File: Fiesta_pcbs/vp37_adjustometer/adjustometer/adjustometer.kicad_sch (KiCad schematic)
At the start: 25 parts, among them J1 VP37 connector, J2 Output, Q1 BC547, Q2 2SK107, U1 UA78M08, U2 RP2040 Micro

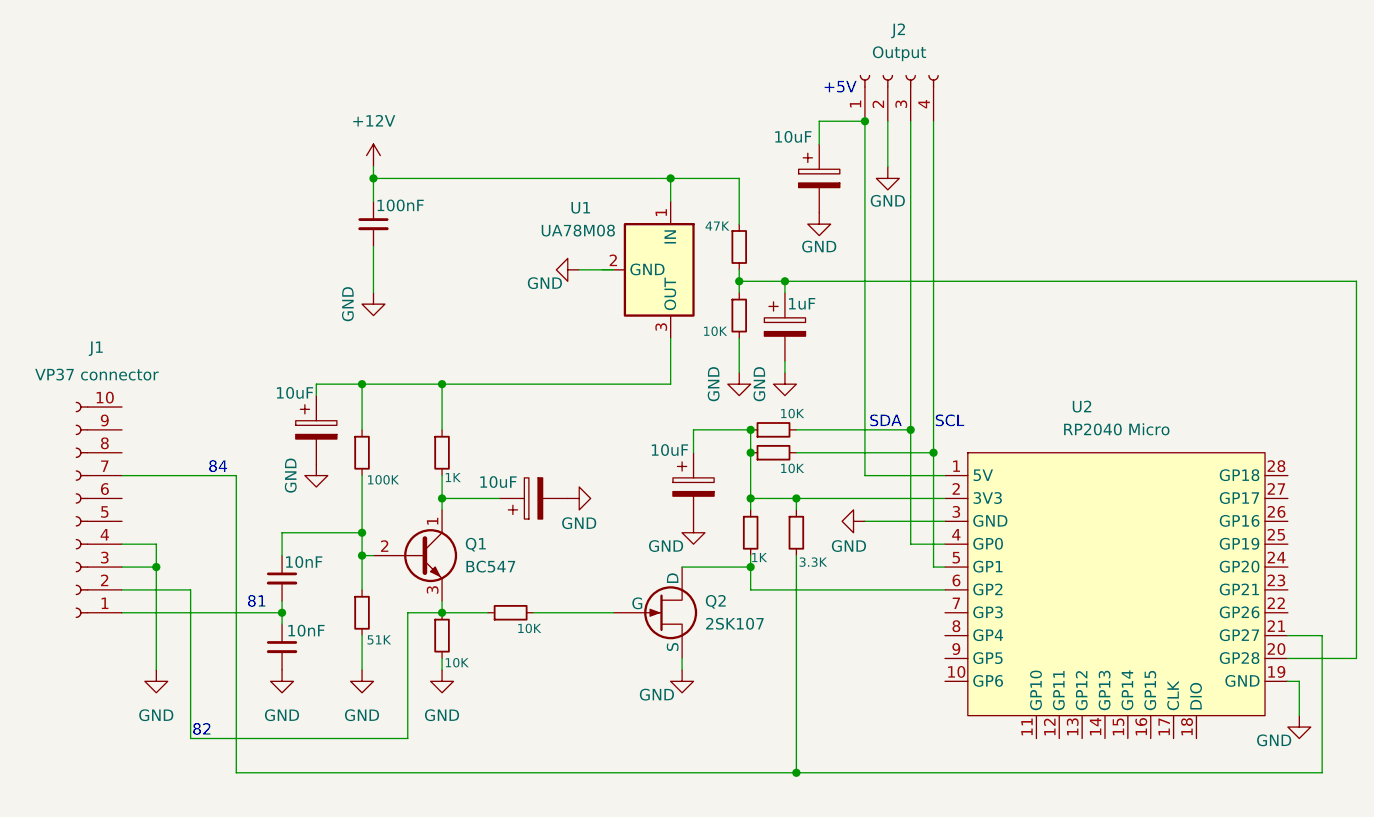
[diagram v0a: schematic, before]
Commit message: sensors, led, start: bitmask status, sequence LED, i2c detection via transaction_count, thermal comp guard
sensors.h/sensors.c:
- Replace AdjStatus enum with bitmask defines: ADJ_STATUS_OK (0x00),
  SIGNAL_LOST (bit 0), FUEL_TEMP_BROKEN (bit 1), BASELINE_PENDING
  (bit 2), VOLTAGE_BAD (bit 3). Multiple bits can be set simultaneously.
- getAdjustometerStatus() returns uint8_t bitmask; checks signal loss,
  baseline readiness, fuel temp raw == 0, and supply voltage outside
  8.0–15.0 V (ADJ_VOLTAGE_MIN_TV / ADJ_VOLTAGE_MAX_TV).
- Thermal compensation now skipped entirely when the fuel temperature
  sensor is broken (raw == ADJ_FUEL_TEMP_SENSOR_BROKEN). Both the EMA
  update and the drift correction are inside the validity guard to
  prevent stale smoothed values from corrupting the drift model.

start.c:
- updateI2CRegisters() reverted to void.
- updateLed() called separately with no arguments.

led.c:
- Detect real I2C activity via hal_i2c_slave_get_transaction_count().
- LED displays a color sequence built additively from active fault
  conditions, each step 500 ms: purple (FUEL_TEMP_BROKEN) and/or red
  (no I2C transactions since last call), always followed by green.
  Signal lost overrides all patterns with 4x/s red blink.
- Steady green at 50% brightness only when all conditions are clear.

config.h: STATUS register comment updated to "status bitmask".

README.md: STATUS register documented as bitmask table with bit
descriptions; LED section updated with combined-sequence behavior.
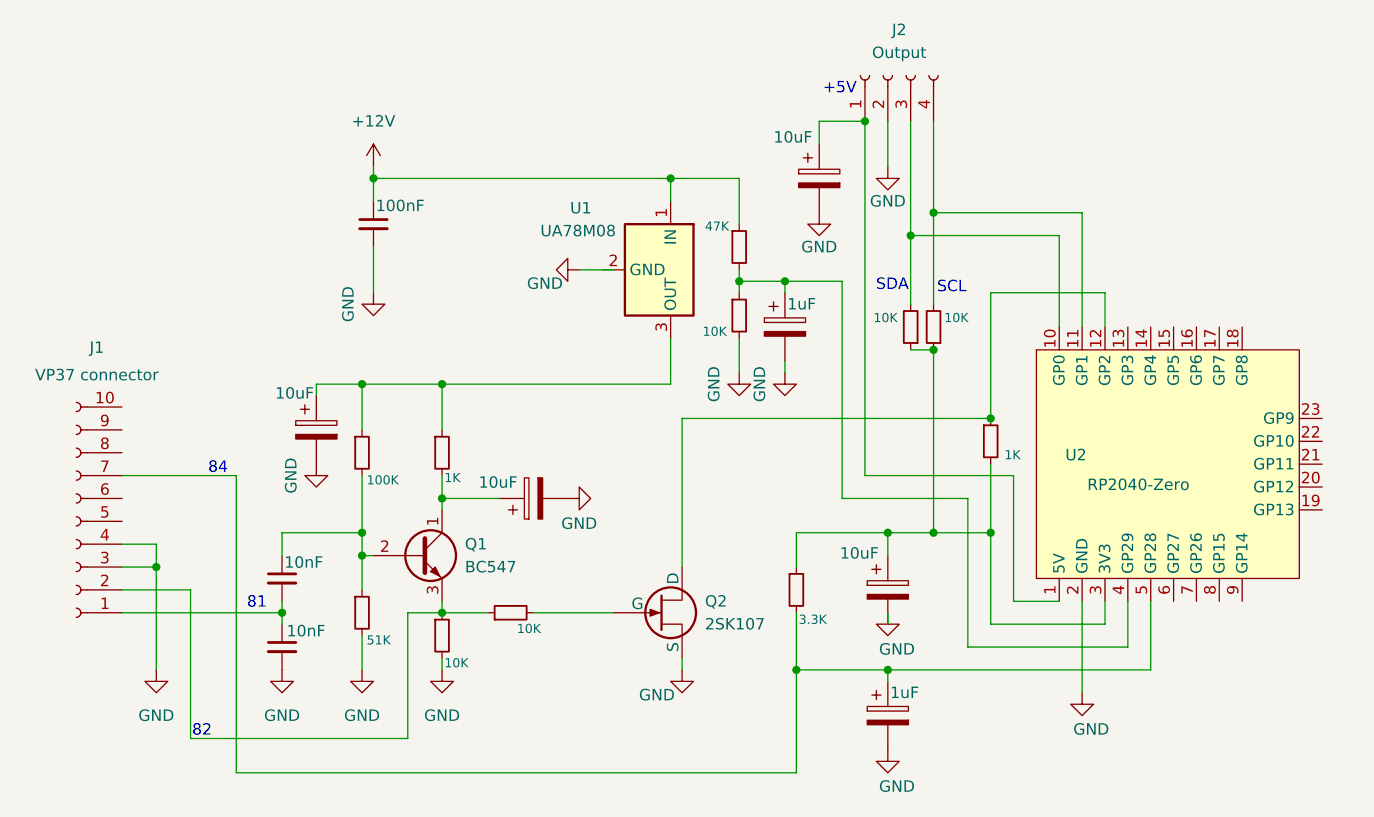
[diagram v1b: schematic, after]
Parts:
- removed 10K (x2): R_Small, symbol Device:R_Small
- added 10K (x2): R_Small, symbol Device:R_Small
- added 1uF: C_Polarized, symbol Device:C_Polarized
- U2: value RP2040 Micro -> RP2040-Zero
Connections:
- net GND: now also U2.2 (GND), 1uF.2; no longer U2.19 (GND), U2.3 (GND)
- net at 10K.1, 1uF.1, 47K.2: now also U2.4 (GP29); no longer U2.20 (GP28)
- net at 10uF.1, 3.3K.1: now also 1K.2, U2.3 (3V3), 10K.1, 10K.1; no longer 1K.1, U2.2 (3V3)
- net at U2.5 (GP28): now also 3.3K.2, J1.7 (Pin_7), 1uF.1; no longer J2.4 (Pin_4)
- net at U2.10 (GP0): now also J2.3 (Pin_3), 10K.2
- net at U2.11 (GP1): now also J2.4 (Pin_4), 10K.2
- net at U2.12 (GP2): now also 1K.1, Q2.1 (D)
- now unconnected: U2.21 (GP27), U2.6 (GP2)
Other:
- moved on the sheet: 3.3K
